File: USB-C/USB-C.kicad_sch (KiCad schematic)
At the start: 6 parts, among them J1 USB_C_Receptacle_USB2.0, U1 USBLC6-2SC6

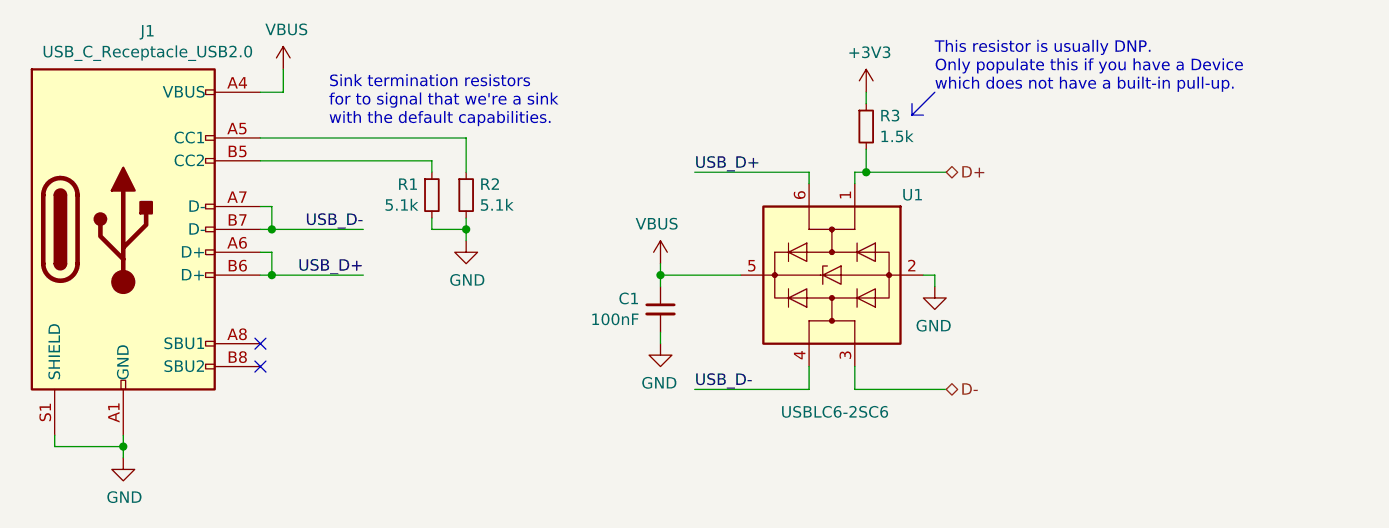
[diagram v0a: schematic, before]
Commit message: Revert "Update modules to kicad v7 format"
This reverts commit 3325eb02d48d3d222bc7f8945228a1814ae85736.
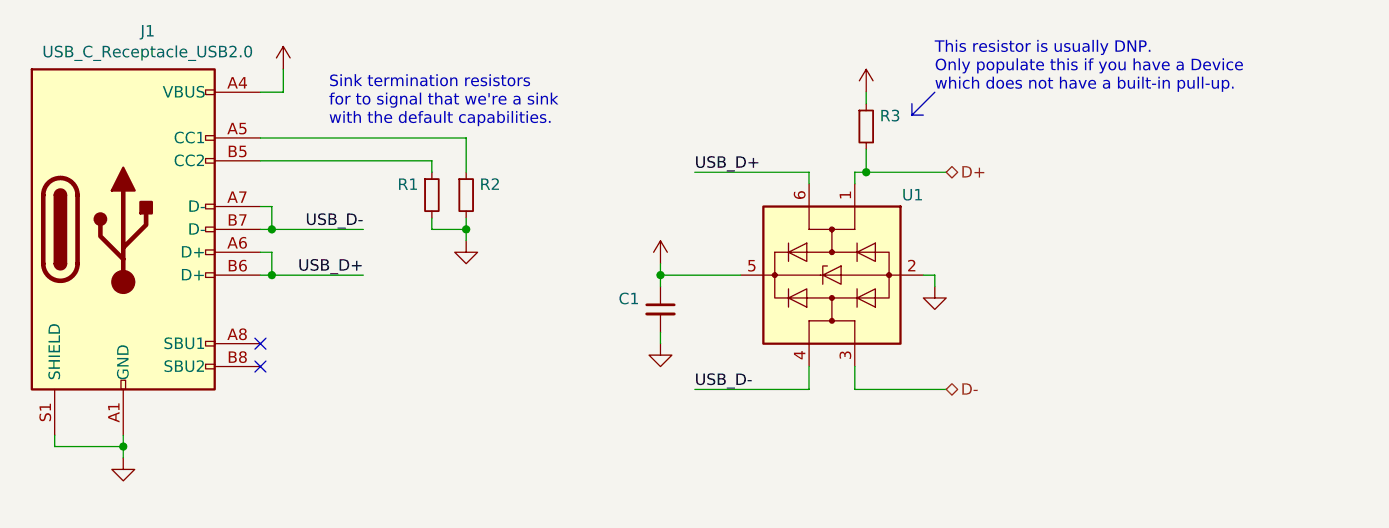
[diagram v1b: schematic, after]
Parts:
- C1: value 100nF -> (none); footprint Capacitor_SMD:C_0402_1005Metric -> (none)
- R1, R2: value 5.1k -> (none); footprint Resistor_SMD:R_0402_1005Metric -> (none)
- R3: value 1.5k -> (none); footprint Resistor_SMD:R_0603_1608Metric -> (none)
- U1: value USBLC6-2SC6 -> (none); footprint Package_TO_SOT_SMD:SOT-23-6 -> (none)

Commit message: Reapply "Update modules to kicad v7 format"
This reverts commit fa5cc85431189ac7a3beedf0871b5723203ae43f.
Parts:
- C1: value (none) -> 100nF; footprint (none) -> Capacitor_SMD:C_0402_1005Metric
- R1, R2: value (none) -> 5.1k; footprint (none) -> Resistor_SMD:R_0402_1005Metric
- R3: value (none) -> 1.5k; footprint (none) -> Resistor_SMD:R_0603_1608Metric
- U1: value (none) -> USBLC6-2SC6; footprint (none) -> Package_TO_SOT_SMD:SOT-23-6
